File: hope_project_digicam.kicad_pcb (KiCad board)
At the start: 2 copper layers, 31 parts, among them J1 USB_C_Receptacle, J2 SD_Card_Port, J3 Camera_Pin_Out, J4 Lipo batt in, J5 TFT_Pin_Socket, J6 extra, Q1 SC-59_SHK, Q2 SOT-23-3L_AOS, SW2 Reset, SW3 Boot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

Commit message: fixed footprints
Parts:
- added R13: 10k, HOPE DigiCam:10k_Res, F.Cu at (178.7, 106.0)
- added SW1: SW_Push, HOPE DigiCam:SW2_SW3, F.Cu at (98.3, 108.2)
- added TP1: TestPoint, TestPoint:TestPoint_Plated_Hole_D2.0mm, F.Cu at (81.6, 106.8)
- added TP10: TestPoint, TestPoint:TestPoint_Plated_Hole_D2.0mm, F.Cu at (86.2, 125.4)
- added TP11: TestPoint, TestPoint:TestPoint_Plated_Hole_D2.0mm, F.Cu at (90.9, 106.8)
- added TP12: TestPoint, TestPoint:TestPoint_Plated_Hole_D2.0mm, F.Cu at (90.9, 111.4)
- added TP13: TestPoint, TestPoint:TestPoint_Plated_Hole_D2.0mm, F.Cu at (90.9, 116.1)
- added TP2: TestPoint, TestPoint:TestPoint_Plated_Hole_D2.0mm, F.Cu at (81.6, 111.4)
- added TP3: TestPoint, TestPoint:TestPoint_Plated_Hole_D2.0mm, F.Cu at (81.6, 116.1)
- added TP4: TestPoint, TestPoint:TestPoint_Plated_Hole_D2.0mm, F.Cu at (81.6, 120.7)
- added TP5: TestPoint, TestPoint:TestPoint_Plated_Hole_D2.0mm, F.Cu at (81.6, 125.4)
- added TP6: TestPoint, TestPoint:TestPoint_Plated_Hole_D2.0mm, F.Cu at (86.2, 106.8)
- added TP7: TestPoint, TestPoint:TestPoint_Plated_Hole_D2.0mm, F.Cu at (86.2, 111.4)
- added TP8: TestPoint, TestPoint:TestPoint_Plated_Hole_D2.0mm, F.Cu at (86.2, 116.1)
- added TP9: TestPoint, TestPoint:TestPoint_Plated_Hole_D2.0mm, F.Cu at (86.2, 120.7)
- J1: value USB_C_Receptacle -> USB_C_Receptacle_USB2.0_16P
- J3: footprint HOPE DigiCam:40_Pin_Conn -> Connector_PinSocket_2.54mm:PinSocket_2x09_P2.54mm_Vertical
- J5: footprint HOPE DigiCam:40_Pin_Conn -> Connector_PinSocket_2.54mm:PinSocket_1x11_P2.54mm_Vertical
- Q1: value SC-59_SHK -> NMOS
- Q2: value SOT-23-3L_AOS -> PMOS
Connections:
- J2 pad CD: unconnected-(J2-PadCD) -> Net-(J2-PadCD)
- J2 pad WP: unconnected-(J2-PadWP) -> Net-(J2-PadCD)

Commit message: Add files via upload
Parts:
- C4, C5, C6, J2, R1, R10, R11, R13, R2, R3, R7, R8, R9, SW2, SW3, U1: moved to B.Cu
- D2: footprint HOPE DigiCam:Shottky_Diode -> Diode_SMD:D_SOD-123
- J1: footprint HOPE DigiCam:USB_C_Receptacle -> Connector_USB:USB_C_Receptacle_GCT_USB4085; moved to B.Cu
- J3: footprint Connector_PinSocket_2.54mm:PinSocket_2x09_P2.54mm_Vertical -> HOPE DigiCam:Cam Module
- J5: footprint Connector_PinSocket_2.54mm:PinSocket_1x11_P2.54mm_Vertical -> HOPE DigiCam:TFT Module; moved to B.Cu
- J6: footprint HOPE DigiCam:40_Pin_Conn -> Connector_PinSocket_2.54mm:PinSocket_1x02_P2.54mm_Vertical
- SW1: value SW_Push -> Cam Trigger
- moved TP13 104.8 mm to (181.9, 64.0)
- moved TP6 94.5 mm to (172.1, 67.3)
- moved J6 93.4 mm to (116.2, 55.9), turned to 0 degrees
- moved TP12 89.0 mm to (172.1, 74.9)
- moved SW3 88.7 mm to (104.1, 65.4), turned to 0 degrees
- moved TP5 87.6 mm to (168.9, 118.7)
- moved J5 87.1 mm to (112.3, 95.5), turned to 0 degrees
- moved TP10 86.9 mm to (162.6, 83.8)
- moved TP1 82.9 mm to (163.2, 92.1)
- moved J1 73.4 mm to (159.5, 59.3)
- moved J4 60.3 mm to (87.0, 101.2), turned to 90 degrees
- moved D1 58.4 mm to (194.4, 57.2), turned to 180 degrees
- moved TP9 58.3 mm to (123.8, 76.2)
- moved D2 58.0 mm to (106.7, 103.4), turned to 90 degrees
- moved R12 55.9 mm to (111.8, 103.1)
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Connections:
- R2 pad 2: Net-(J1-CC1) -> /CC1
- R3 pad 2: Net-(J1-CC2) -> /CC2
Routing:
- net +3.3V: track 243.3 -> 88.4 mm, vias 11 -> 0
- net /CAM_SDA: track 110.6 -> 0.00 mm, vias 4 -> 0
- net /CAM_SCL: track 106.0 -> 0.00 mm, vias 4 -> 0
- net /CAM_VS: track 84.0 -> 0.00 mm, vias 4 -> 0
- net /VBUS: track 30.1 -> 103.4 mm, vias 2 -> 1
- net /CAM_HS: track 69.0 -> 0.00 mm, vias 6 -> 0
- net /CAM_PC: track 61.9 -> 0.00 mm, vias 4 -> 0
- net /SD_CS: track 68.4 -> 6.68 mm, vias 2 -> 0
- net /CAM_XC: track 60.3 -> 0.00 mm, vias 4 -> 0
- net /CAM_D9: track 57.4 -> 0.00 mm
- net /CAM_D8: track 57.1 -> 0.00 mm
- net /CAM_D7: track 55.4 -> 0.00 mm
- net /CAM_D6: track 53.7 -> 0.00 mm
- net /CAM_D5: track 52.1 -> 0.00 mm
- net /CAM_D4: track 50.5 -> 0.00 mm
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- added copper zone on F.Cu, net +3.3V
- added copper zone on B.Cu, net GND
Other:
- board outline added: 127 x 71.1 mm

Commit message: finished layout pretty much
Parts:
- removed TP10, TP11, TP12, TP7, TP8, TP9: TestPoint, TestPoint:TestPoint_Plated_Hole_D2.0mm
- J1, SW2, SW3: moved to F.Cu
- SW1: footprint HOPE DigiCam:SW2_SW3 -> SWITCH_CAM:D6R_CNK
- moved D1 100.9 mm to (93.5, 56.5)
- moved TP2 100.3 mm to (186.8, 62.5)
- moved J4 99.5 mm to (178.0, 61.0), turned to 0 degrees
- moved R5 96.5 mm to (93.0, 59.5), turned to 0 degrees
- moved TP3 92.1 mm to (186.8, 67.8)
- moved Q1 90.9 mm to (99.0, 59.0), turned to -90 degrees
- moved Q2 88.3 mm to (181.5, 67.7), turned to 180 degrees
- moved TP5 85.3 mm to (93.0, 79.8)
- moved R6 82.4 mm to (103.0, 58.5), turned to -90 degrees
- moved D2 79.3 mm to (177.5, 67.7)
- moved R4 77.0 mm to (105.5, 58.5), turned to 90 degrees
- moved C2 71.7 mm to (186.0, 74.0)
- moved R12 71.3 mm to (173.5, 67.4)
- moved TP13 71.2 mm to (111.0, 57.0)
- moved U3 70.3 mm to (181.5, 74.0)
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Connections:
- U1 pad 10: /CAM_D8 -> /CAM_D4
- U1 pad 11: /CAM_D9 -> /CAM_D5
- U1 pad 12: /CAM_PC -> /CAM_D6
- U1 pad 15: /CAM_XC -> /CAM_D7
- U1 pad 16: /TFT_DC -> /CAM_D8
- U1 pad 17: /TFT_CS -> /CAM_D9
- U1 pad 18: /SD_CS -> /CAM_XC
- U1 pad 19: /SD_MOSI -> /CAM_PC
- U1 pad 20: /SD_SCK -> /CAM_HS
- U1 pad 21: /SD_MISO -> /CAM_VS
- U1 pad 22: /CAM_TRIGGER -> /CAM_SDA
- U1 pad 23: /CAM_HS -> /CAM_SCL
- U1 pad 24: /CAM_VS -> /TFT_LIT
- U1 pad 25: /TFT_LIT -> /TFT_DC
- U1 pad 26: /LED -> unconnected-(U1-IO45-Pad26)
- U1 pad 31: /TFT_SCK -> /TFT_CS
- U1 pad 33: unconnected-(U1-IO40-Pad33) -> /LED
- U1 pad 38: /CAM_SDA -> /TFT_SCK
- U1 pad 39: /CAM_SCL -> /CAM_TRIGGER
- U1 pad 4: /CAM_D2 -> /SD_MISO
- U1 pad 5: /CAM_D3 -> /SD_SCK
- U1 pad 6: /CAM_D4 -> /SD_MOSI
- U1 pad 7: /CAM_D5 -> /SD_CS
- U1 pad 8: /CAM_D6 -> /CAM_D2
- U1 pad 9: /CAM_D7 -> /CAM_D3
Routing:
- net /VBUS: track 103.4 -> 29.8 mm, vias 1 -> 0
- net /CAM_D3: track 0.00 -> 53.7 mm
- net /CAM_D2: track 0.00 -> 52.3 mm
- net /CAM_D5: track 0.00 -> 50.3 mm
- net /SD_CS: track 6.68 -> 55.8 mm
- net /CAM_D4: track 0.00 -> 49.0 mm
- net +3.3V: track 88.4 -> 41.3 mm, vias 0 -> 3
- net /CAM_D6: track 0.00 -> 45.4 mm
- net /CAM_VS: track 0.00 -> 43.9 mm
- net /CAM_PC: track 0.00 -> 43.9 mm
- net /CAM_SCL: track 0.00 -> 43.9 mm
- net /CAM_D9: track 0.00 -> 43.9 mm
- net /CAM_D7: track 0.00 -> 43.9 mm
- net /SD_MOSI: track 10.2 -> 53.7 mm
- net /CAM_HS: track 0.00 -> 40.8 mm
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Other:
- board size 127 x 71.1 mm -> 114.2 x 67 mm

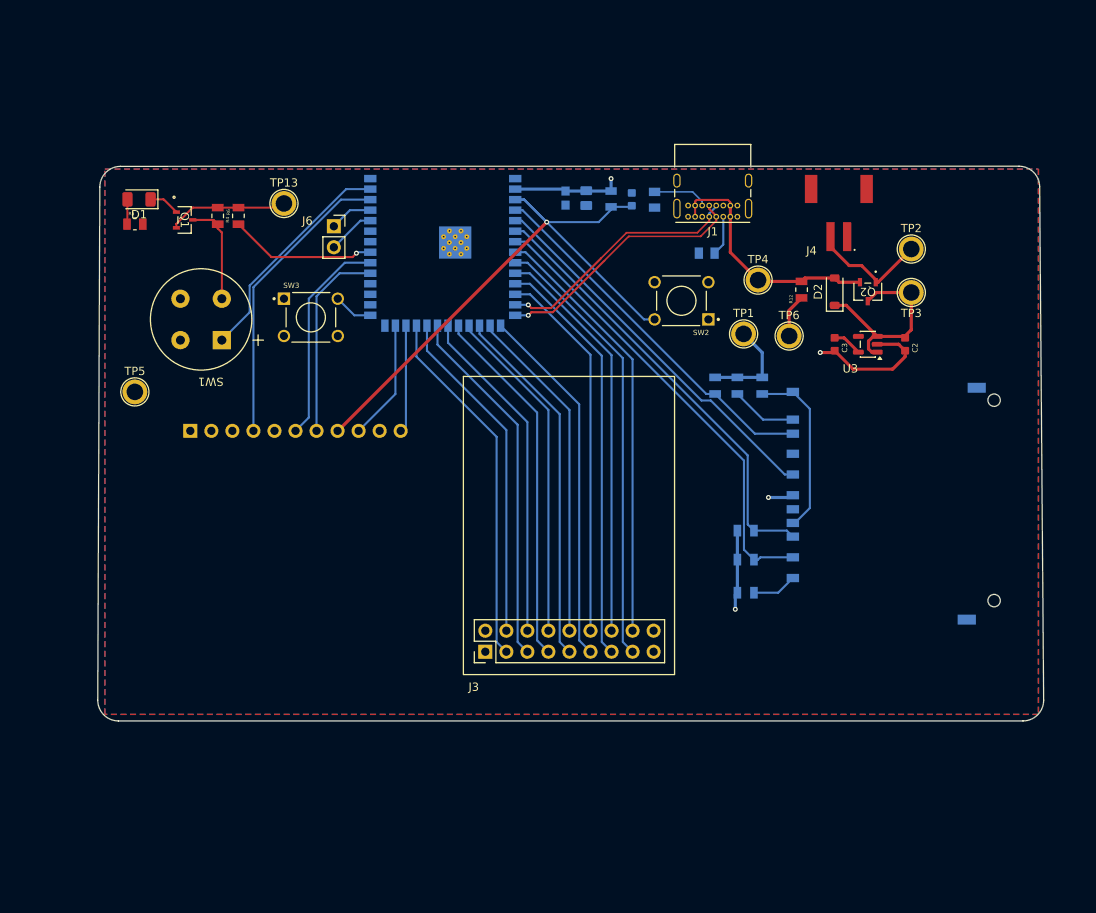
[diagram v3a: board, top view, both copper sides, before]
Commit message: made silkscreen more readable
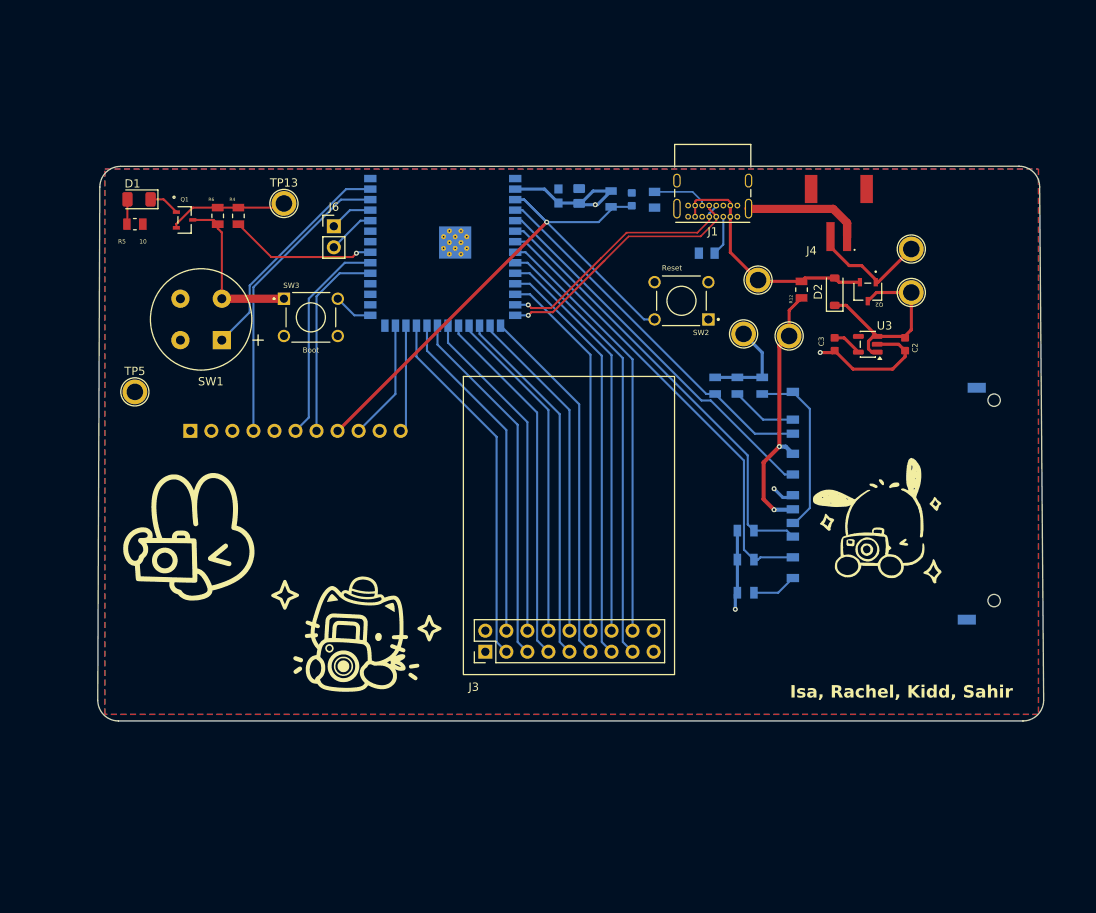
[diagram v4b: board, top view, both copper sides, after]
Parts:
- added G***: LOGO, LOGO, F.Cu at (99.7, 97.2)
- added G***: LOGO, LOGO, F.Cu at (119.4, 109.2)
- added G***: LOGO, LOGO, F.Cu at (183.5, 95.9)
- J6: footprint Connector_PinSocket_2.54mm:PinSocket_1x02_P2.54mm_Vertical -> Connector_PinHeader_2.54mm:PinHeader_1x02_P2.54mm_Vertical
- TP1 +3.3V: renamed from TP1
- TP2 +BATT: renamed from TP2
- TP3 PWR_IN: renamed from TP3
- TP4 VBUS: renamed from TP4
- TP6 GND: renamed from TP6
- moved C5 0.89 mm to (144.1, 56.1), turned to 90 degrees
- moved C6 0.89 mm to (146.6, 56.1), turned to 90 degrees
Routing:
- net GND: track 34.2 -> 82.8 mm, vias 1 -> 3
- net +3.3V: track 41.3 -> 45.4 mm
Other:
- board text added: "Isa, Rachel, Kidd, Sahir"
